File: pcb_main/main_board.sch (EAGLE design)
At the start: 54 parts, among them Q1 FDS5680, T1 BC847, U1 STM32F411RET6, X1 FH12-14S-0.5SH

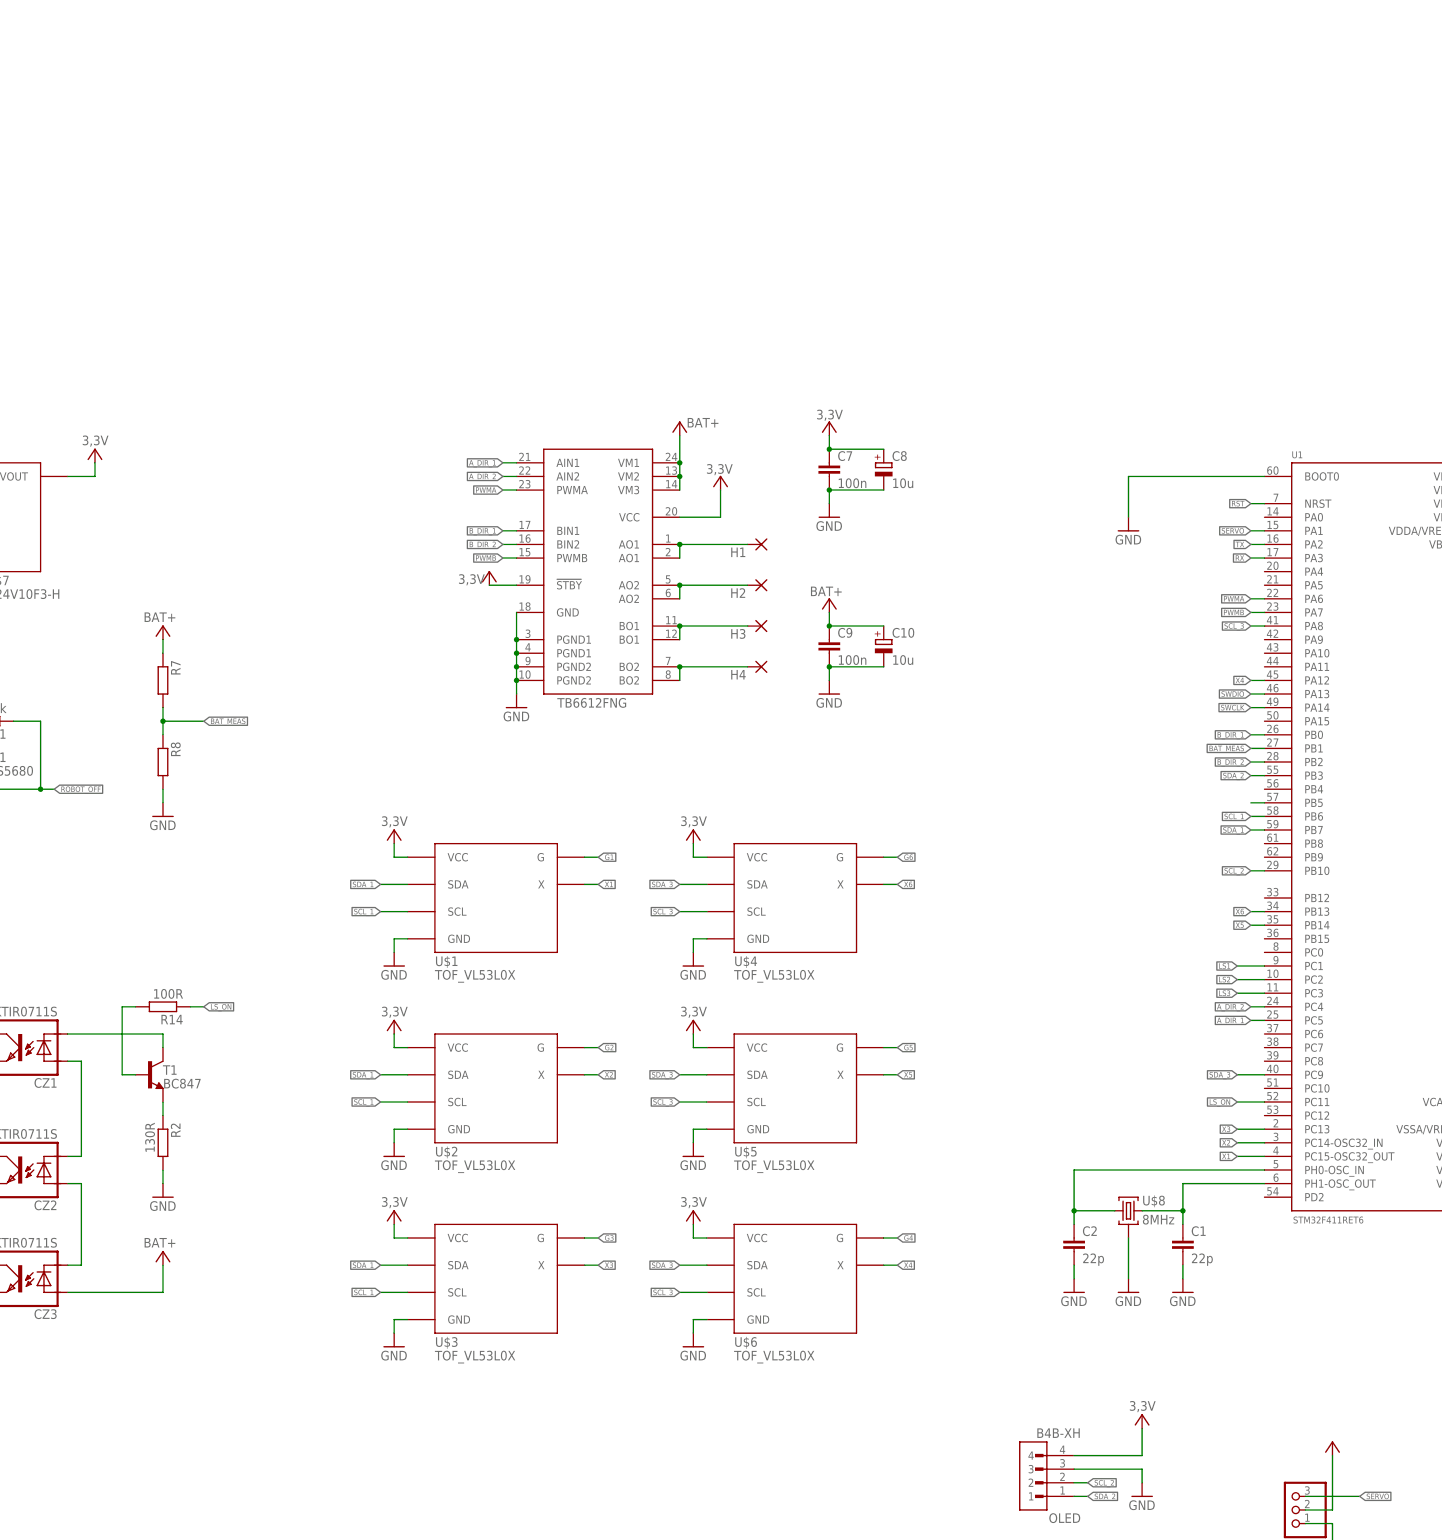
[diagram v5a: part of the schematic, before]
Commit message: 2 h-bridges, 5V reg
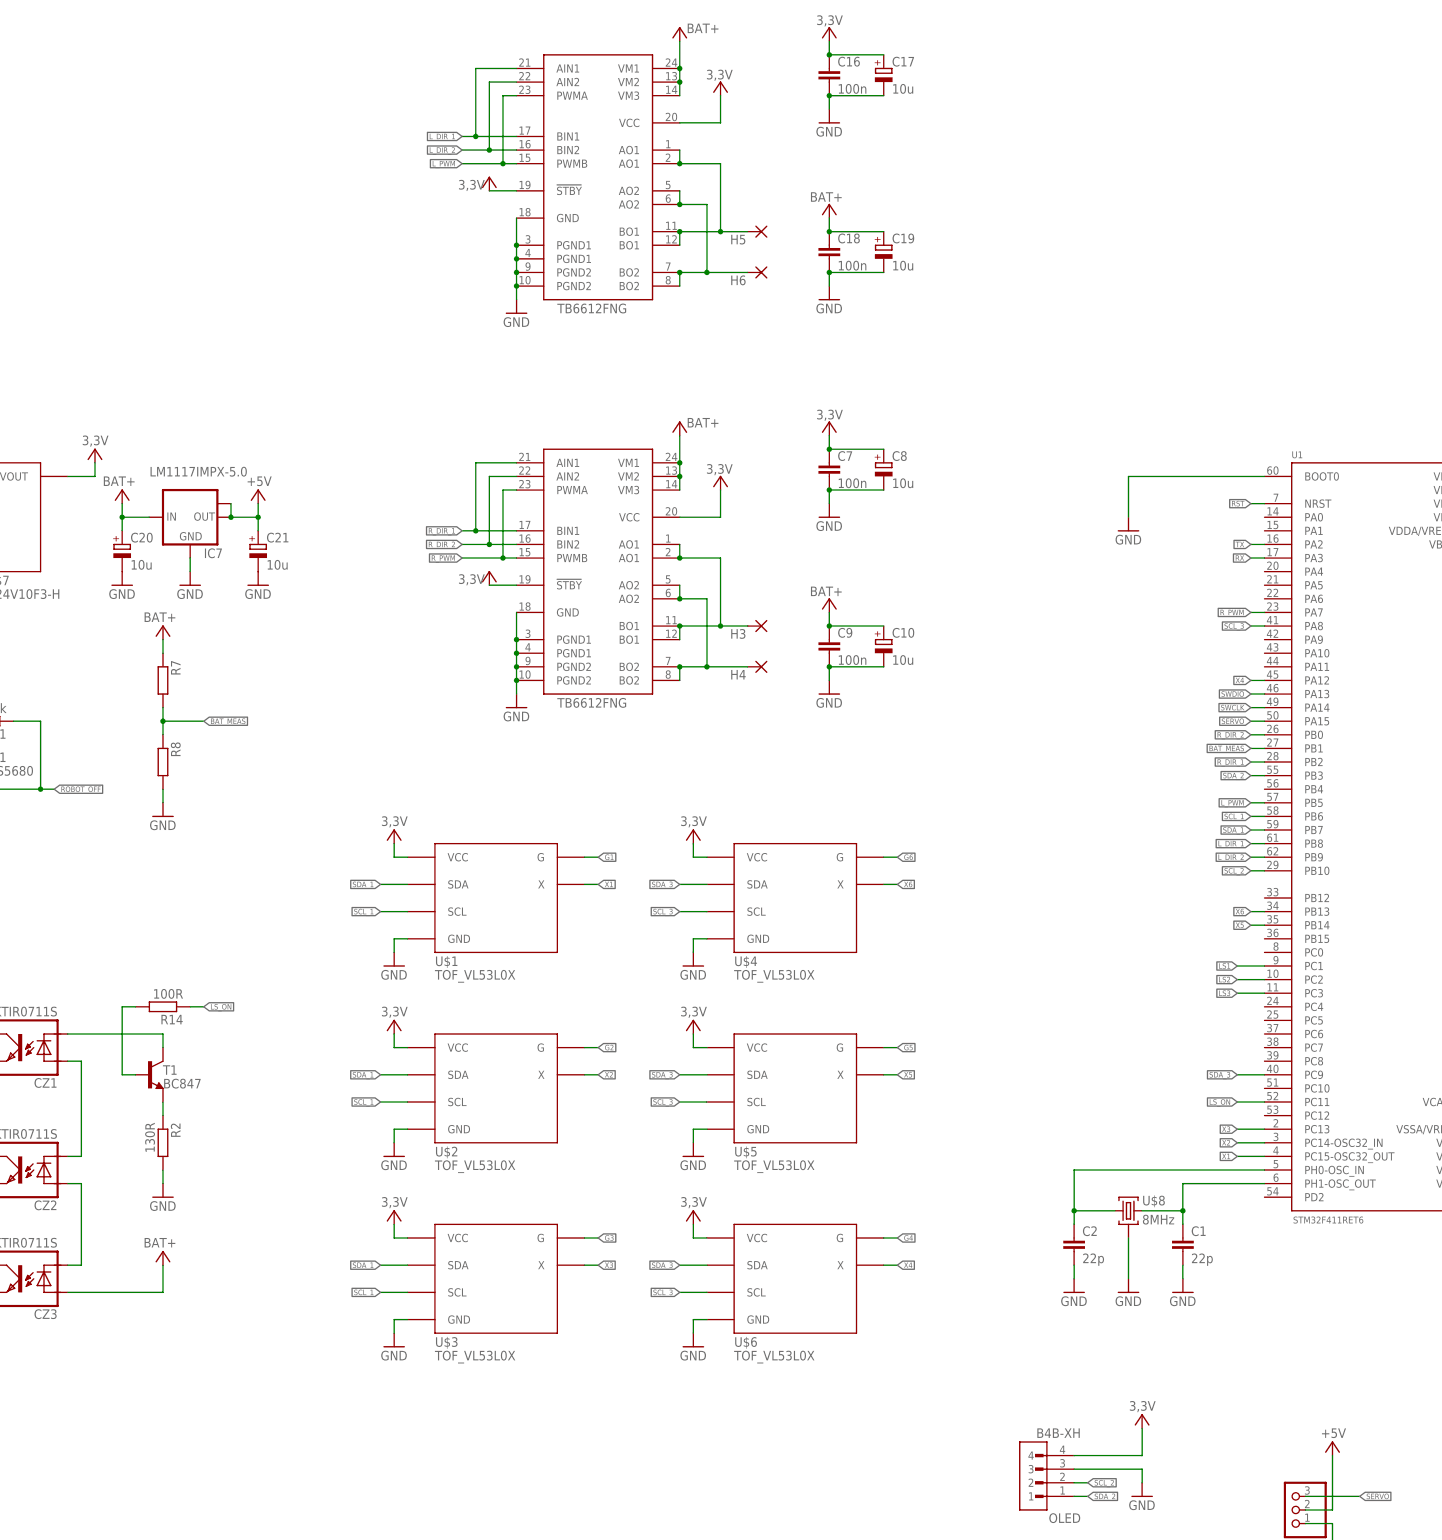
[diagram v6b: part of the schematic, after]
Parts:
- removed H1, H2: (no value), wirepad:1,6/0,8
- added C16, C18: 100n, rcl:C-EUC0603
- added C17, C19, C20, C21: 10u, rcl:CPOL-EUB/3528-21W
- added H5, H6: (no value), wirepad:1,6/0,8
- added IC7: LM1117IMPX-5.0, lm1117:LM1117IMPX-5.0
- added TB6612_: TB6612FNG, tb6612:TB6612FNG
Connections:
- removed net AO: H1.P, TB6612.AO1@1, TB6612.AO1@2
- removed net AO2: H2.P, TB6612.AO2@1, TB6612.AO2@2
- removed net A_DIR_1: TB6612.AIN1, U1.PC5
- removed net A_DIR_2: TB6612.AIN2, U1.PC4
- removed net B_DIR_1: TB6612.BIN1, U1.PB0
- removed net B_DIR_2: TB6612.BIN2, U1.PB2
- removed net N$7: U1.PB5
- removed net PWMA: TB6612.PWMA, U1.PA6
- removed net PWMB: TB6612.PWMB, U1.PA7
- removed net VCC: JP1.2
- new net +5V: C21.+, IC7.OUT, IC7.OUT1, JP1.2
- new net BO3: H5.P, TB6612_.AO1@1, TB6612_.AO1@2, TB6612_.BO1@1, TB6612_.BO1@2
- new net BO4: H6.P, TB6612_.AO2@1, TB6612_.AO2@2, TB6612_.BO2@1, TB6612_.BO2@2
- new net L_DIR_1: TB6612_.AIN1, TB6612_.BIN1, U1.PB8
- new net L_DIR_2: TB6612_.AIN2, TB6612_.BIN2, U1.PB9
- new net L_PWM: TB6612_.PWMA, TB6612_.PWMB, U1.PB5
- new net R_DIR_1: TB6612.AIN1, TB6612.BIN1, U1.PB2
- new net R_DIR_2: TB6612.AIN2, TB6612.BIN2, U1.PB0
- new net R_PWM: TB6612.PWMA, TB6612.PWMB, U1.PA7
- net 3,3V: now also C16.1, C17.+, TB6612_.!STBY, TB6612_.VCC
- net BAT+: now also C18.1, C19.+, C20.+, IC7.IN, TB6612_.VM1, TB6612_.VM2, TB6612_.VM3
- net BO1: now also TB6612.AO1@1, TB6612.AO1@2
- net BO2: now also TB6612.AO2@1, TB6612.AO2@2
- net GND: now also C16.2, C17.-, C18.2, C19.-, C20.-, C21.-, IC7.GND, TB6612_.GND, TB6612_.PGND1@1, TB6612_.PGND1@2, TB6612_.PGND2@1, TB6612_.PGND2@2
- net SERVO: now also U1.PA15; no longer U1.PA1

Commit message: almost done
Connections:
- net R_PWM: now also U1.PA6; no longer U1.PA7
- net X6: now also U1.PC5; no longer U1.PB13
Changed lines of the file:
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@@
 </segment>
 <segment>
-<pinref part="U1" gate="G$1" pin="PB13"/>
-<wire x1="-2.54" y1="-17.78" x2="-5.08" y2="-17.78" width="0.1524" layer="91"/>
-<label x="-5.08" y="-17.78" size="1.016" layer="95" rot="R180" xref="yes"/>
+<wire x1="-2.54" y1="-38.1" x2="-5.08" y2="-38.1" width="0.1524" layer="91"/>
+<label x="-5.08" y="-38.1" size="1.016" layer="95" rot="R180" xref="yes"/>
+<pinref part="U1" gate="G$1" pin="PC5"/>
 </segment>
 </net>
@@
 </segment>
 <segment>
-<pinref part="U1" gate="G$1" pin="PA7"/>
-<wire x1="-2.54" y1="38.1" x2="-5.08" y2="38.1" width="0.1524" layer="91"/>
-<label x="-5.08" y="38.1" size="1.016" layer="95" rot="R180" xref="yes"/>
-</segment>
-</net>
+<wire x1="-2.54" y1="40.64" x2="-5.08" y2="40.64" width="0.1524" layer="91"/>
+<label x="-5.08" y="40.64" size="1.016" layer="95" rot="R180" xref="yes"/>
+<pinref part="U1" gate="G$1" pin="PA6"/>
+</segment>
+</net>

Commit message: main pcb done
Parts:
- removed JP1: (no value), pinhead:PINHD-1X3
- added LED1, LED2: (no value), led:LEDCHIPLED_0603
- added R16: 1k?, rcl:R-EU_R0603
- added R17: 470R?, rcl:R-EU_R0603
- added SERVO: (no value), pinhead:PINHD-1X3
- R15: value 130R -> 10k
- R3, R4, R5: value (none) -> 4k7
- R7: value (none) -> 33k?
- R8: value (none) -> 10k
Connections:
- removed net +5V: C21.+, IC7.OUT, IC7.OUT1, JP1.2
- new net 5V: C21.+, IC7.OUT, IC7.OUT1, LED1.A, SERVO.2
- new net N$1: LED1.C, R16.1
- new net N$7: LED2.C, R17.1
- new net STARTER: U1.PB12, X1-2.1
- net 3,3V: now also LED2.A
- net GND: now also R16.2, R17.2, SERVO.1; no longer JP1.1
- net LED: now also U1.PB13
- net RX: now also X1-3.1
- net SERVO: now also SERVO.3; no longer JP1.3
- net SW1: now also U1.PC4
- net SW2: now also U1.PA7
- net SW3: now also U1.PA5
- net SW4: now also U1.PA4
- net TX: now also X1-4.1
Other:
- note added: "Connectors"
- note removed: "dodać złącze na serwo, kondensatory pullupy do i2c uart"
- moved on the sheet: BATT, C10, C16, C17, C18, C19, C20, C21, C7, C8, C9, CZ1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
